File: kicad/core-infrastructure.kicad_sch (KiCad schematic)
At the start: 8 parts, among them J2 T-Connector Deans 14 AWG, SW2 Latching Push Button, U5 PCA9685PW, U6 JZK 2S 7.4V 8A BMS, U7 MP1584 Buck Converter 5V, U8 ESP32-S3 Super Mini

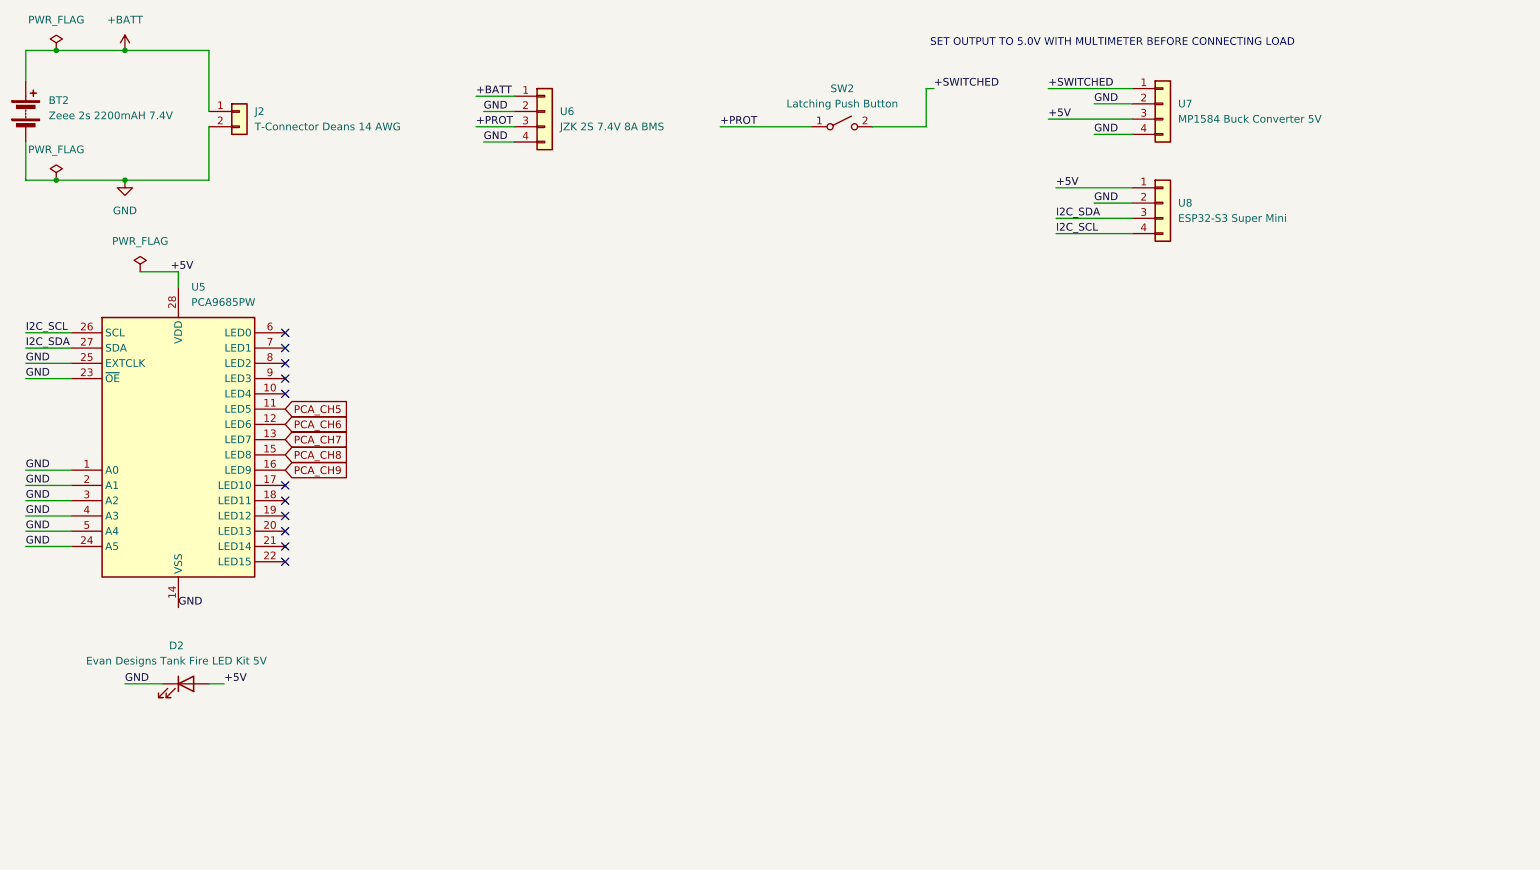
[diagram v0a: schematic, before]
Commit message: docs: rename schematic sheets and add SVG exports
- Rename core-power.kicad_sch → core-infrastructure.kicad_sch
- Rename blaster-zones.kicad_sch → blaster.kicad_sch
- Export core-infrastructure.svg and blaster.svg from KiCad
- Update SVG references in core-infrastructure.md and blaster.md
- Update CLAUDE.md schematic table to reflect new filenames

Closes #21

Co-Authored-By: Claude Sonnet 4.6 <noreply@anthropic.com>
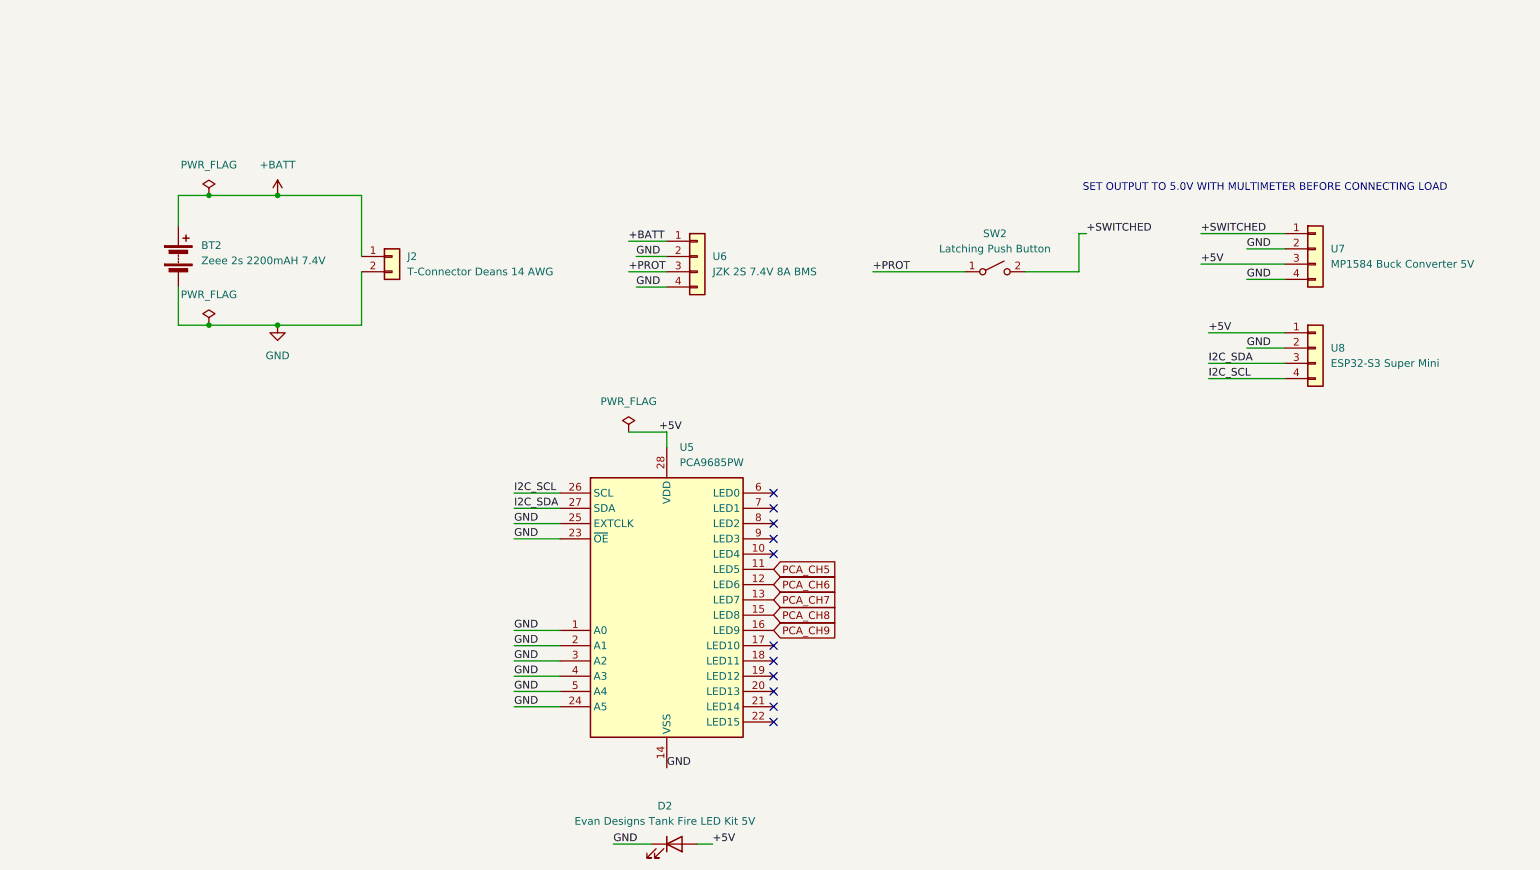
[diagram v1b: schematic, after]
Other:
- title: Core Power -> Core Infrastructure
- moved on the sheet: BT2, D2, J2, SW2, U5, U6, U7, U8

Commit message: docs: expand build guide with breadboard prototype plan (#27)
* docs: expand build guide with step-by-step breadboard prototype plan

Each step includes wiring instructions and explicit pass/fail criteria.
Steps 1-2 (power chain setup) are actionable now; steps 3-6 are marked
as waiting on the ESP32-S3.

Co-Authored-By: Claude Sonnet 4.6 <noreply@anthropic.com>

* docs: update BMS status to Arrived in core infrastructure BOM

Co-Authored-By: Claude Sonnet 4.6 <noreply@anthropic.com>

* docs: simplify power chain — remove BMS, add low-voltage alarm

- Remove BMS from power chain; battery internal protection is sufficient
  for this low-current display application
- Add LiPo low-voltage alarm on JST-XH balance lead for overdischarge warning
- Update wire gauge table to reflect battery → switch → buck chain
- Note that switch pre-soldered leads (~26 AWG) must be replaced with
  14 AWG stranded wire
- Simplify build guide Steps 1-2 to match new power chain
- Update core-infrastructure schematic and re-export SVG

Co-Authored-By: Claude Sonnet 4.6 <noreply@anthropic.com>

* docs: remove BMS references from all docs and update schematic

Removes stale BMS component, net labels, and power chain diagram from
schematic-progress.md; updates torso.md, core-infrastructure.md, and
CLAUDE.md to reflect the simplified power chain (lipo → switch → buck →
5V bus). Also includes the updated KiCad schematic and SVG export.

* docs: document switch current headroom math in core infrastructure

* docs: update blaster with measured current draw and MOSFET explanation

- Mark MOSFET and series resistor as Arrived in BOM
- Add explanation of why a MOSFET is needed (PCA9685 25mA limit vs 300mA rope)
- Replace theoretical Note with measured 72mA draw at 5V through 6.8Ω
- Note resistor sizing revisit deferred to later prototype phase

Co-Authored-By: Claude Sonnet 4.6 <noreply@anthropic.com>

* docs: correct LED rope current draw and remove redundant MOSFET justification

Actual measured draw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
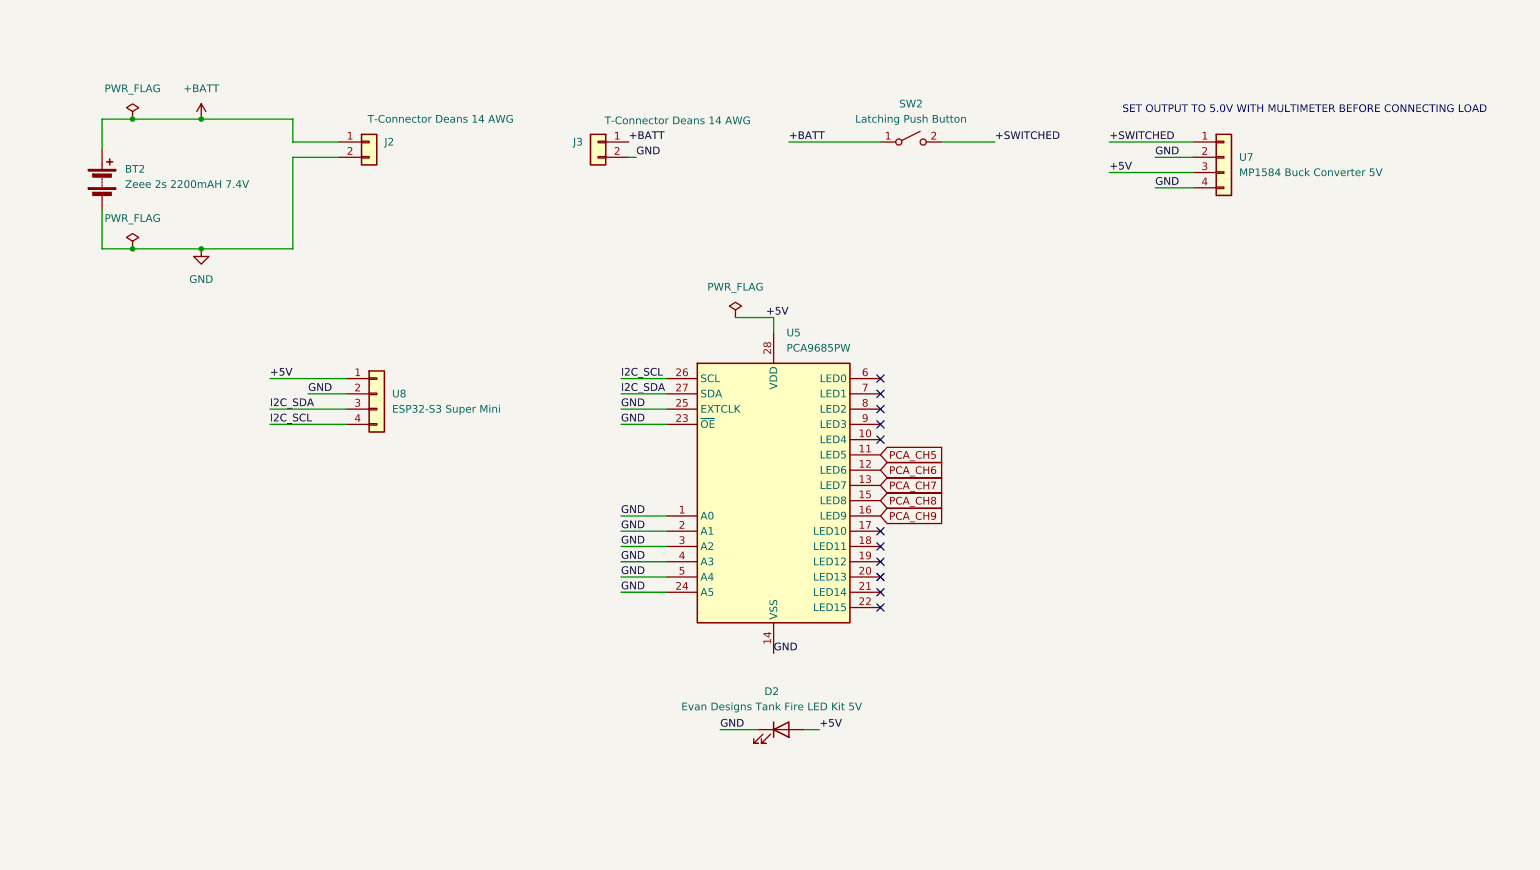
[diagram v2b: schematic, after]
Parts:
- removed U6: JZK 2S 7.4V 8A BMS, symbol Connector_Generic:Conn_01x04
- added J3: T-Connector Deans 14 AWG, symbol Connector_Generic:Conn_01x02
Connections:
- net +PROT is gone; now on net +BATT: SW2.1 (A)
- net +BATT: now also J3.1 (Pin_1)
- net GND: now also J3.2 (Pin_2)
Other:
- moved on the sheet: BT2, D2, J2, SW2, U5, U7, U8

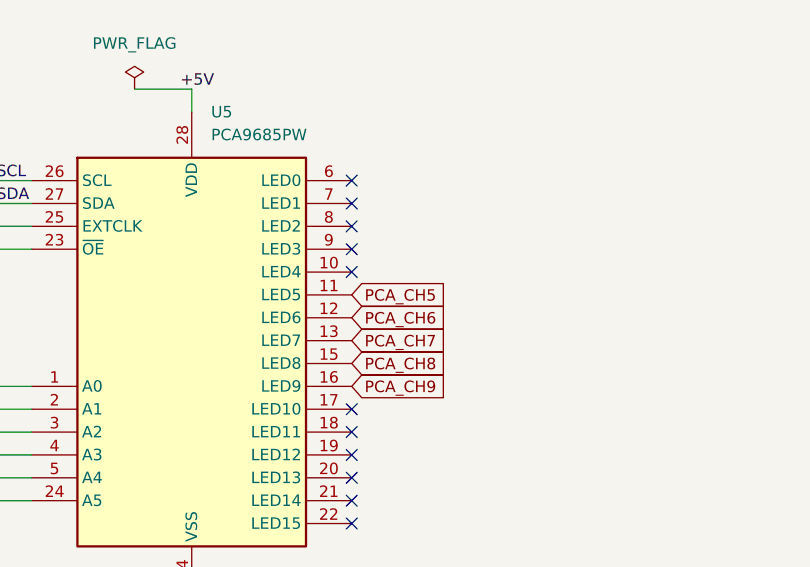
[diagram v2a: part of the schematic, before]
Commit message: feat: blaster schematic update and heatsink sequence prototype (#39)
* feat: add heatsink firing sequence prototype sketch (step-d5)

Co-Authored-By: Claude Sonnet 4.6 <noreply@anthropic.com>

* docs: update wire gauge to Kynar 28 AWG OFHC for all internal wiring

Co-Authored-By: Claude Sonnet 4.6 <noreply@anthropic.com>

* feat: update blaster schematic, channel map, and heatsink sequence

- Reverse heatsink channel order: Ch 1 = front, Ch 5 = rear (reactor end)
- Update blaster.kicad_sch: resistor values, channel labels, zone names
- Regenerate blaster.svg and core-infrastructure.svg from KiCad
- Update docs (blaster.md, channel-map.md, arms.md) to reflect new channel order
- Update step-d5 firmware defines and discharge direction
- Update CLAUDE.md schematic status

Co-Authored-By: Claude Sonnet 4.6 <noreply@anthropic.com>

---------

Co-authored-by: Claude Sonnet 4.6 <noreply@anthropic.com>
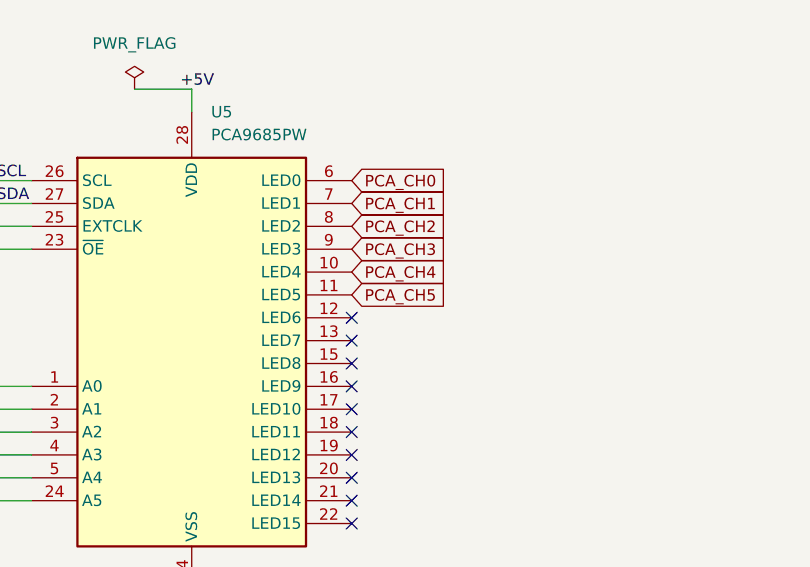
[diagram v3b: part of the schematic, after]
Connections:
- net PCA_CH4: now reaches U5.10 (LED4)
- net PCA_CH0: now reaches U5.6 (LED0)
- net PCA_CH1: now reaches U5.7 (LED1)
- net PCA_CH2: now reaches U5.8 (LED2)
- net PCA_CH3: now reaches U5.9 (LED3)
- net PCA_CH6: no longer names the net of U5.12 (LED6)
- net PCA_CH7: no longer names the net of U5.13 (LED7)
- net PCA_CH8: no longer names the net of U5.15 (LED8)
- net PCA_CH9: no longer names the net of U5.16 (LED9)
- no-connect marks 11 -> 10
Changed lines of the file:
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@@
 	)
 	(no_connect
-		(at 163.83 93.98)
+		(at 163.83 104.14)
+	)
+	(no_connect
+		(at 163.83 101.6)
 	)
 	(no_connect
@@
 	)
 	(no_connect
+		(at 163.83 106.68)
+	)
+	(no_connect
 		(at 163.83 111.76)
 	)
 	(no_connect
-		(at 163.83 83.82)
-	)
-	(no_connect
-		(at 163.83 91.44)
-	)
-	(no_connect
-		(at 163.83 88.9)
+		(at 163.83 99.06)
 	)
 	(no_connect
 		(at 163.83 119.38)
-	)
-	(no_connect
-		(at 163.83 86.36)
 	)
 	(no_connect
@@
 		)
 	)
-	(global_label "PCA_CH6"
+	(global_label "PCA_CH3"
 		(shape input)
-		(at 163.83 99.06 0)
+		(at 163.83 91.44 0)
 		(fields_autoplaced yes)
 		(effects
@@
 		)
 		(property "Intersheetrefs" "${INTERSHEET_REFS}"
-			(at 175.2214 99.06 0)
+			(at 175.2214 91.44 0)
+			(hide yes)
+			(show_name no)
+			(do_not_autoplace no)
+			(effects
+				(font
+					(size 1.27 1.27)
+				)
+				(justify left)
+			)
+		)
+	)
+	(global_label "PCA_CH1"
+		(shape input)
+		(at 163.83 86.36 0)
+		(fields_autoplaced yes)
+		(effects
+			(font
+				(size 1.27 1.27)
+			)
+			(justify left)
+		)
+		(property "Intersheetrefs" "${INTERSHEET_REFS}"
+			(at 175.2214 86.36 0)
+			(hide yes)
+			(show_name no)
+			(do_not_autoplace no)
+			(effects
+				(font
+					(size 1.27 1.27)
+				)
+				(justify left)
+			)
+		)
+	)
+	(global_label "PCA_CH2"
+		(shape input)
+		(at 163.83 88.9 0)
+		(fields_autoplaced yes)
+		(effects
+			(font
+				(size 1.27 1.27)
+			)
+			(justify left)
+		)
+		(property "Intersheetrefs" "${INTERSHEET_REFS}"
+			(at 175.2214 88.9 0)
 			(hide yes)
 			(show_name no)
@@
 		)
 	)
-	(global_label "PCA_CH7"
+	(global_label "PCA_CH4"
 		(shape input)
-		(at 163.83 101.6 0)
+		(at 163.83 93.98 0)
 		(fields_autoplaced yes)
 		(effects
@@
 		)
 		(property "Intersheetrefs" "${INTERSHEET_REFS}"
-			(at 175.2214 101.6 0)
+			(at 175.2214 93.98 0)
 			(hide yes)
 			(show_name no)
@@
 		)
 	)
-	(global_label "PCA_CH9"
+	(global_label "PCA_CH0"
 		(shape input)
-		(at 163.83 106.68 0)
+		(at 163.83 83.82 0)
 		(fields_autoplaced yes)
 		(effects
@@
 		)
 		(property "Intersheetrefs" "${INTERSHEET_REFS}"
-			(at 175.2214 106.68 0)
+			(at 175.2214 83.82 0)
 			(hide yes)
 			(show_name no)
-			(do_not_autoplace no)
-			(effects
-				(font
-					(size 1.27 1.27)
-				)
-				(justify left)
-			)
-		)
-	)
-	(global_label "PCA_CH8"
-		(shape input)
-		(at 163.83 104.14 0)
-		(fields_autoplaced yes)
-		(effects
-			(font
-				(size 1.27 1.27)
-			)
-			(justify left)
-		)
-		(property "Intersheetrefs" "${INTERSHEET_REFS}"
-			(at 175.2214 104.14 0)
-			(hide yes)
-			(show_name no)
